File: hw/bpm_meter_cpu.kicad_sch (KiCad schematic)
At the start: 33 parts, among them J1 USB_C_Receptacle_USB2.0, J2 Conn_01x03_Pin, SW2 SW_MEC_5E, U1 RP2040, U3 W25Q128JVS, U4 AMS1117-3.3, Y1 Crystal_GND24_Small

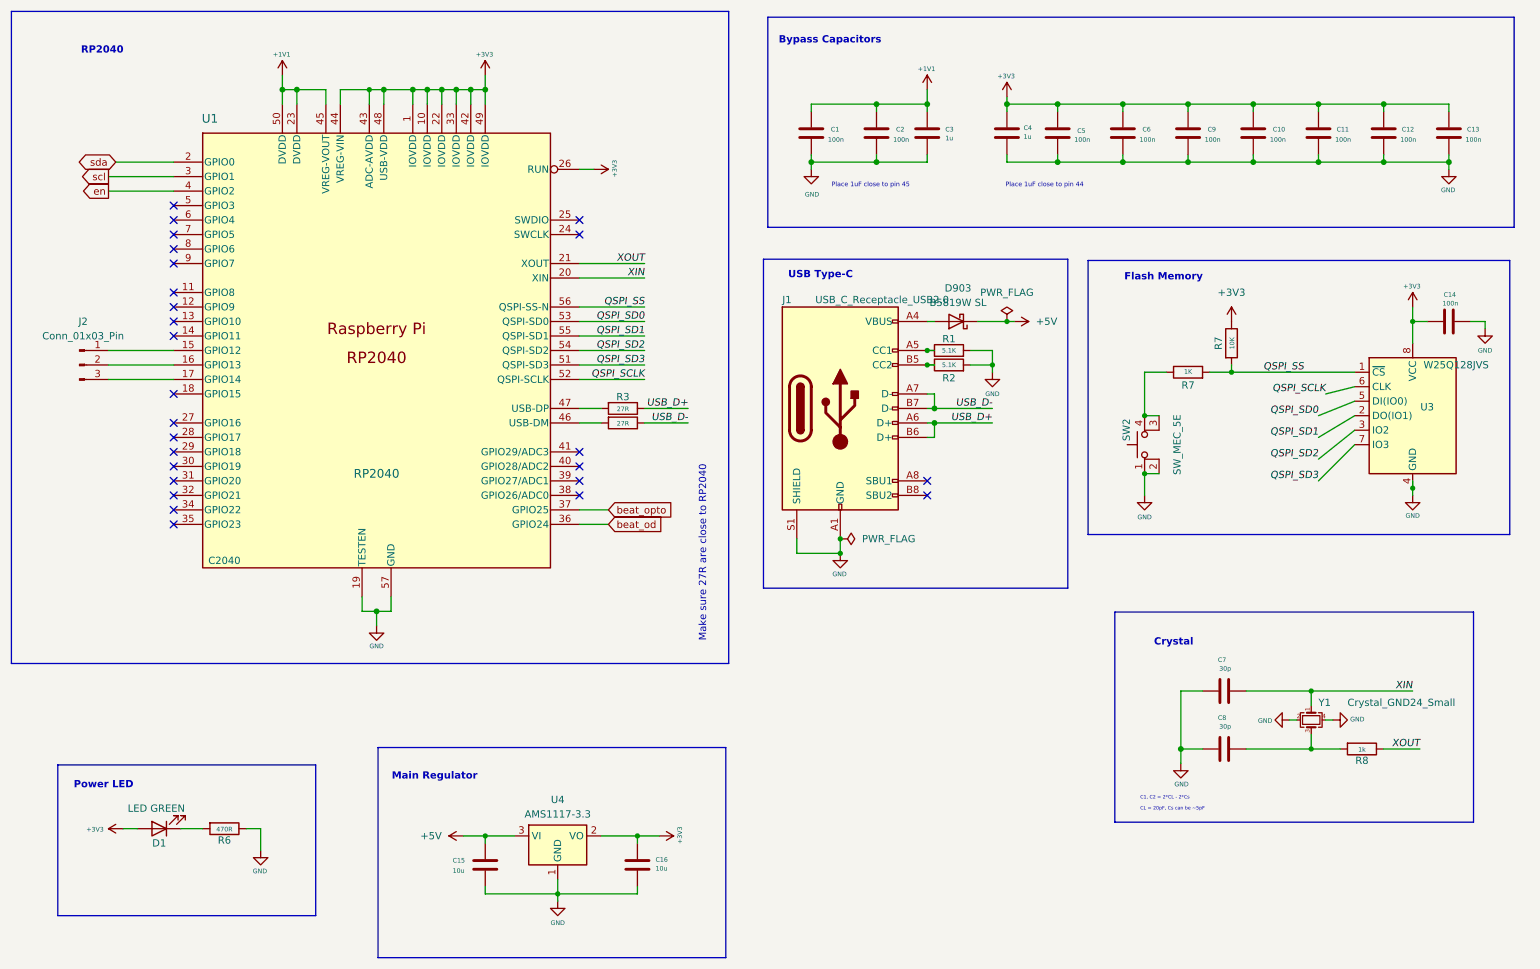
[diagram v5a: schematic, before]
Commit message: Changed LED driver to ISSI IS31FL3236A
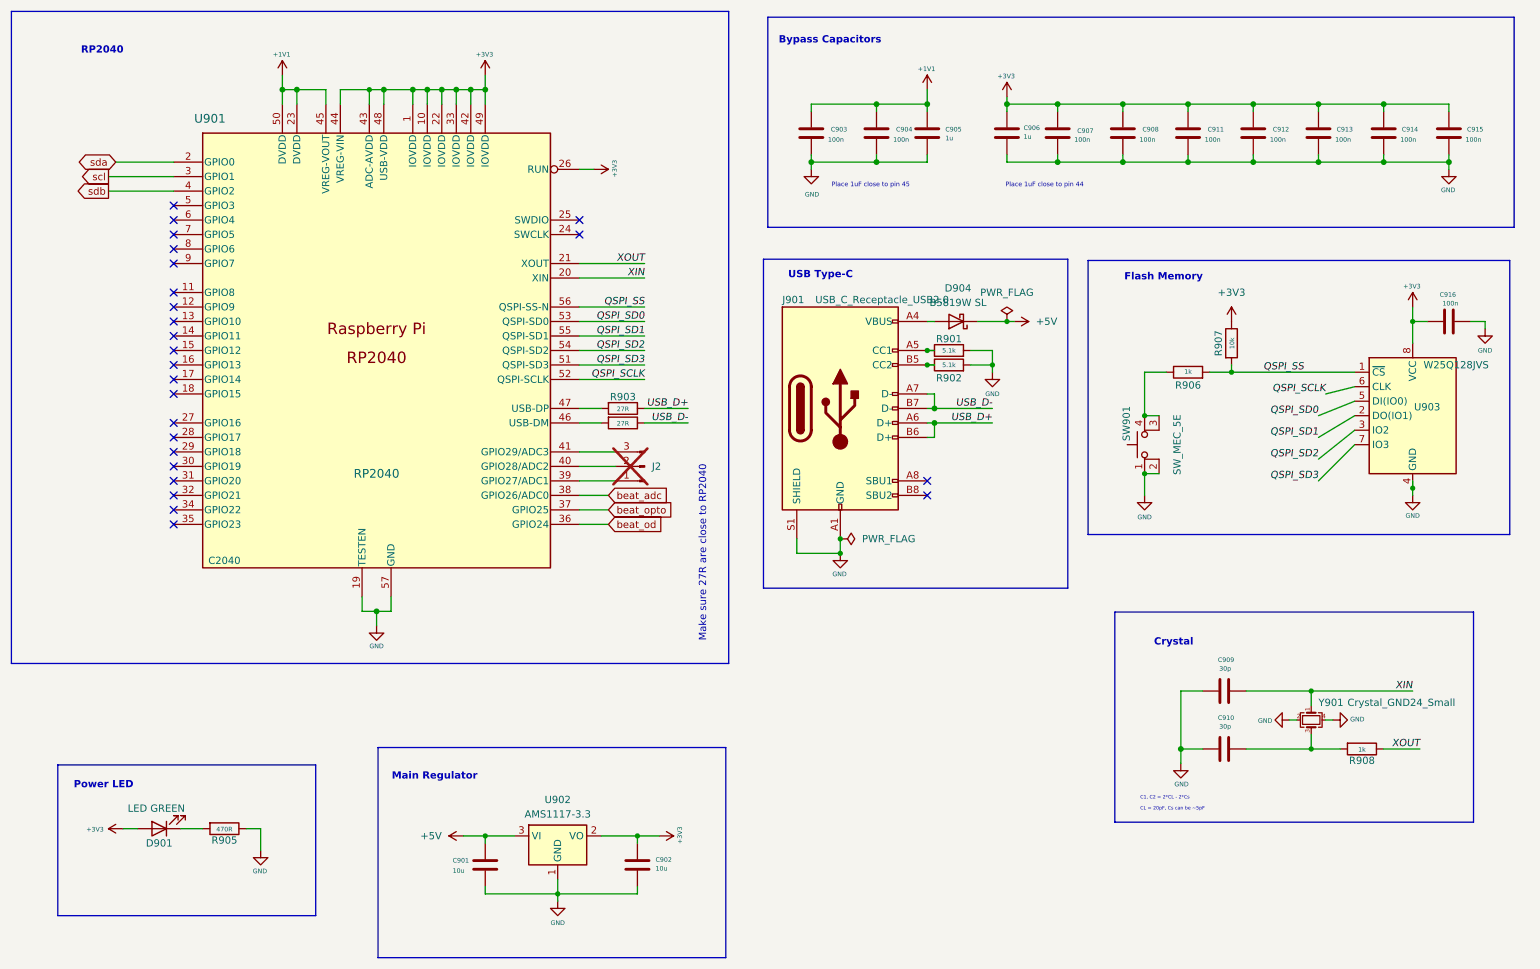
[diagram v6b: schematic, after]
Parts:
- J2: now not fitted
- R901: renamed from R1; value 5.1K -> 5.1k
- R902: renamed from R2; value 5.1K -> 5.1k
- R906: renamed from R7; value 1K -> 1k
- R907: renamed from R7; value 10K -> 10k
- U903: renamed from U3; JCL C97521 -> (none)
- renumbered C15 to C901, C16 to C902, C1 to C903, C2 to C904, C3 to C905, C4 to C906, C5 to C907, C6 to C908, C7 to C909, C8 to C910, C9 to C911, C10 to C912, C11 to C913, C12 to C914, C13 to C915, C14 to C916, D1 to D901, D903 to D904, J1 to J901, R3 to R903, R4 to R904, R6 to R905, R8 to R908, SW2 to SW901, U1 to U901, U4 to U902, Y1 to Y901
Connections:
- net at J2.1 (Pin_1): now also U901.39 (GPIO27/ADC1); no longer U901.15 (GPIO12)
- net at J2.2 (Pin_2): now also U901.40 (GPIO28/ADC2); no longer U901.16 (GPIO13)
- net at J2.3 (Pin_3): now also U901.41 (GPIO29/ADC3); no longer U901.17 (GPIO14)
- net beat_adc: now reaches U901.38 (GPIO26/ADC0)
- net en renamed sdb
- no-connect marks 26 -> 25

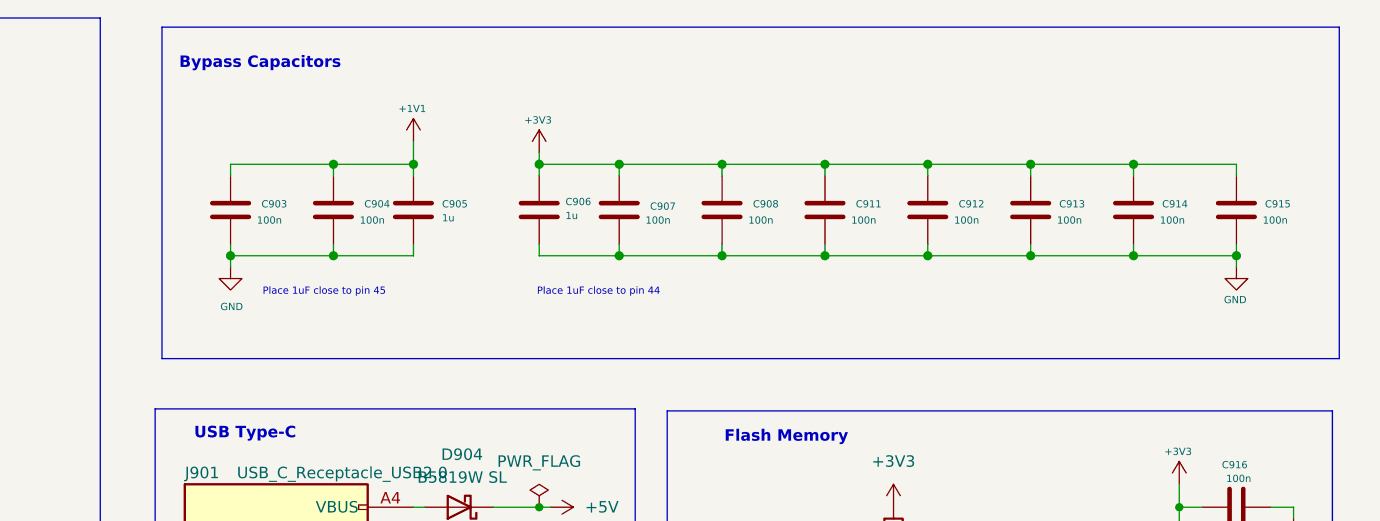
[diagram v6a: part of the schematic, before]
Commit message: Optimized layout of the RP2040
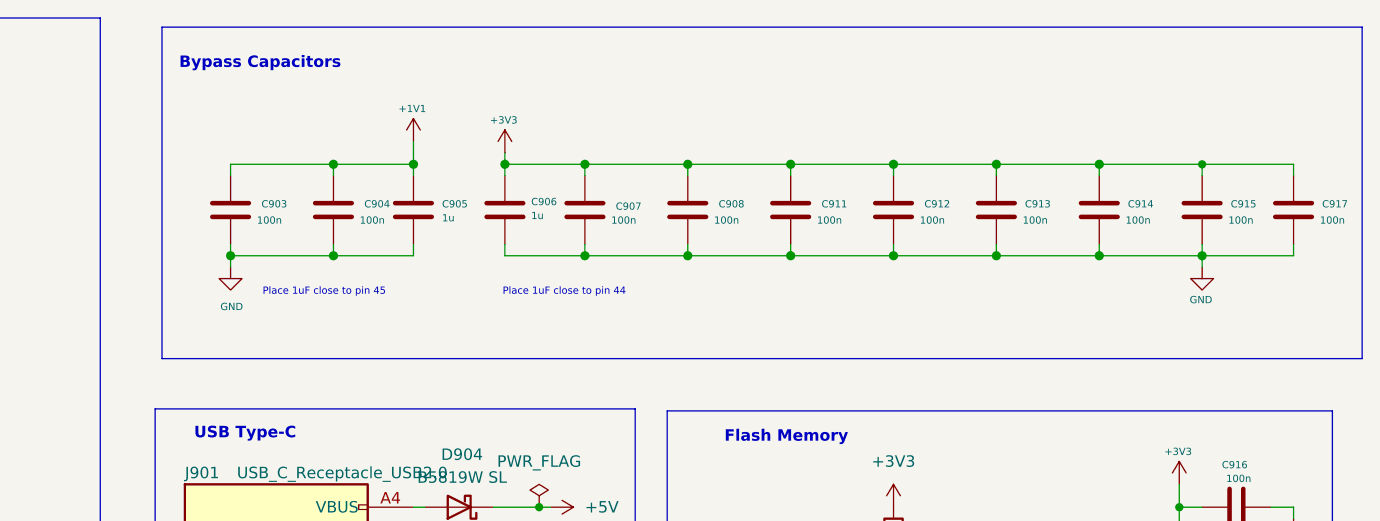
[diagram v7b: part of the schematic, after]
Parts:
- added C917: 100n, Capacitor_SMD:C_0402_1005Metric_Pad0.74x0.62mm_HandSolder, symbol 00_project_library:C
- D901: footprint 00_project_library:LED_0603_1608Metric -> LED_SMD:LED_0805_2012Metric
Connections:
- net +3V3: now also C917.1
- net GND: now also C917.2
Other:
- moved on the sheet: C906, C907, C908, C911, C912, C913, C914, C915

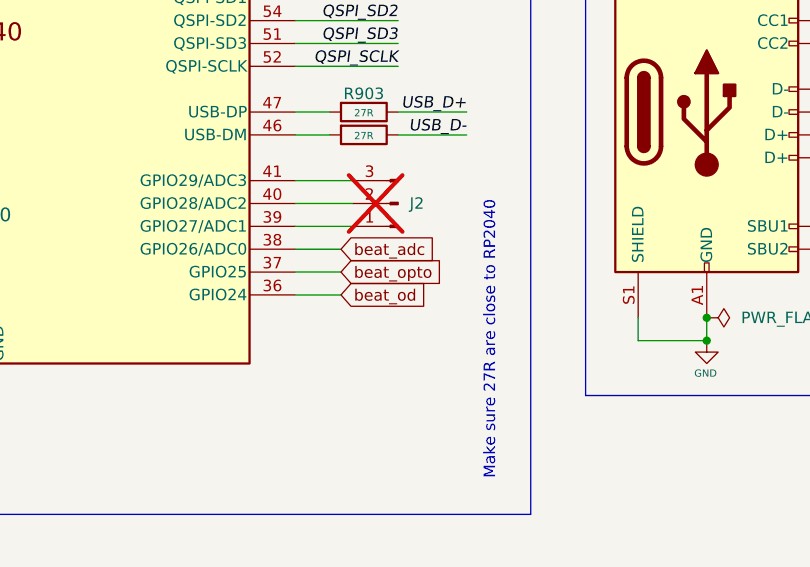
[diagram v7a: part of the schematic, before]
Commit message: Routing almost finished, QSPI flash missing
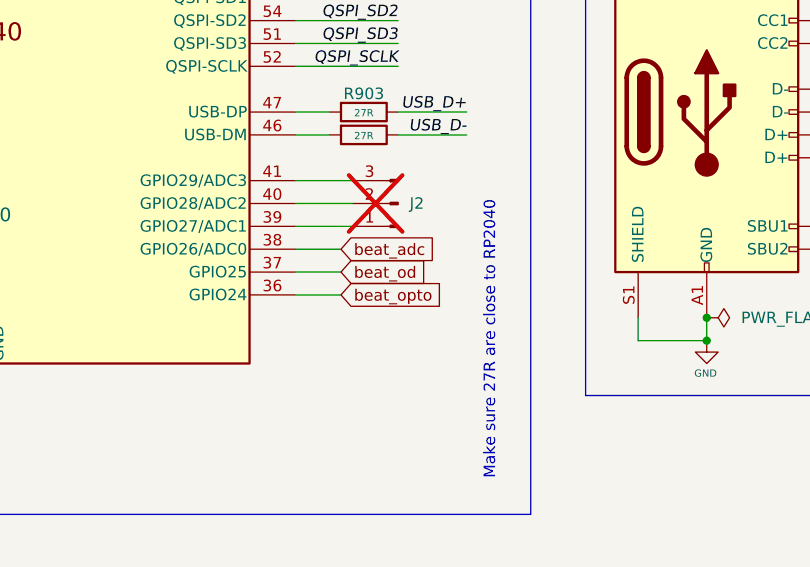
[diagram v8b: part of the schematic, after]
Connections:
- net beat_od: now also U901.37 (GPIO25); no longer U901.36 (GPIO24)
- net beat_opto: now also U901.36 (GPIO24); no longer U901.37 (GPIO25)
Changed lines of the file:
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@@
   (no_connect (at 44.45 100.33))
   (no_connect (at 44.45 74.93))
+  (wire (pts (xy 115.57 105.41) (xy 120.65 105.41))
+    (stroke (width 0) (type default))
+  )
   (wire (pts (xy 99.06 31.75) (xy 99.06 29.21))
     (stroke (width 0) (type solid))
@@
     (stroke (width 0) (type default))
   )
-  (wire (pts (xy 115.57 105.41) (xy 120.65 105.41))
-    (stroke (width 0) (type default))
-  )
   (wire (pts (xy 184.15 74.93) (xy 187.96 74.93))
     (stroke (width 0) (type default))
@@
     (stroke (width 0) (type solid))
   )
+  (wire (pts (xy 63.5 26.67) (xy 63.5 29.21))
+    (stroke (width 0) (type solid))
+  )
+  (wire (pts (xy 66.04 31.75) (xy 66.04 29.21))
+    (stroke (width 0) (type solid))
+  )
+  (wire (pts (xy 274.32 69.85) (xy 274.32 71.12))
+    (stroke (width 0) (type default))
+  )
+  (wire (pts (xy 127 85.09) (xy 134.62 85.09))
+    (stroke (width 0) (type solid))
+  )
+  (wire (pts (xy 77.47 120.65) (xy 77.47 118.11))
+    (stroke (width 0) (type solid))
+  )
+  (wire (pts (xy 214.63 100.33) (xy 214.63 96.52))
+    (stroke (width 0) (type default))
+  )
+  (wire (pts (xy 243.84 142.24) (xy 243.84 144.78))
+    (stroke (width 0) (type default))
+  )
+  (wire (pts (xy 86.36 31.75) (xy 86.36 29.21))
+    (stroke (width 0) (type solid))
+  )
+  (wire (pts (xy 241.3 33.02) (xy 241.3 31.75))
+    (stroke (width 0) (type solid))
+  )
+  (wire (pts (xy 161.29 107.95) (xy 161.29 110.49))
+    (stroke (width 0) (type solid))
+  )
+  (wire (pts (xy 153.67 110.49) (xy 161.29 110.49))
+    (stroke (width 0) (type solid))
+  )
+  (wire (pts (xy 44.45 44.45) (xy 33.02 44.45))
+    (stroke (width 0) (type default))
+  )
+  (wire (pts (xy 251.46 81.28) (xy 246.38 82.55))
+    (stroke (width 0) (type default))
+  )
+  (wire (pts (xy 224.79 144.78) (xy 220.98 144.78))
+    (stroke (width 0) (type solid))
+  )
+  (wire (pts (xy 264.16 33.02) (xy 264.16 31.75))
+    (stroke (width 0) (type solid))
+  )
+  (wire (pts (xy 176.53 29.21) (xy 176.53 31.75))
+    (stroke (width 0) (type solid))
+  )
+  (wire (pts (xy 73.66 31.75) (xy 73.66 29.21))
+    (stroke (width 0) (type solid))
+  )
+  (wire (pts (xy 261.62 67.31) (xy 261.62 69.85))
+    (stroke (width 0) (type solid))
+  )
+  (wire (pts (xy 240.03 139.7) (xy 241.3 139.7))
+    (stroke (width 0) (type default))
+  )
+  (wire (pts (xy 186.69 31.75) (xy 195.58 31.75))
+    (stroke (width 0) (type solid))
+  )
+  (wire (pts (xy 186.69 41.91) (xy 195.58 41.91))
+    (stroke (width 0) (type solid))
+  )
+  (wire (pts (xy 224.79 134.62) (xy 220.98 134.62))
+    (stroke (width 0) (type solid))
+  )
+  (wire (pts (xy 111.76 167.64) (xy 111.76 170.18))
+    (stroke (width 0) (type default))
+  )
   (wire (pts (xy 115.57 102.87) (xy 120.65 102.87))
-    (stroke (width 0) (type default))
-  )
-  (wire (pts (xy 63.5 26.67) (xy 63.5 29.21))
-    (stroke (width 0) (type solid))
-  )
-  (wire (pts (xy 66.04 31.75) (xy 66.04 29.21))
-    (stroke (width 0) (type solid))
-  )
-  (wire (pts (xy 274.32 69.85) (xy 274.32 71.12))
-    (stroke (width 0) (type default))
-  )
-  (wire (pts (xy 127 85.09) (xy 134.62 85.09))
-    (stroke (width 0) (type solid))
-  )
-  (wire (pts (xy 77.47 120.65) (xy 77.47 118.11))
-    (stroke (width 0) (type solid))
-  )
-  (wire (pts (xy 214.63 100.33) (xy 214.63 96.52))
-    (stroke (width 0) (type default))
-  )
-  (wire (pts (xy 243.84 142.24) (xy 243.84 144.78))
-    (stroke (width 0) (type default))
-  )
-  (wire (pts (xy 86.36 31.75) (xy 86.36 29.21))
-    (stroke (width 0) (type solid))
-  )
-  (wire (pts (xy 241.3 33.02) (xy 241.3 31.75))
-    (stroke (width 0) (type solid))
-  )
-  (wire (pts (xy 161.29 107.95) (xy 161.29 110.49))
-    (stroke (width 0) (type solid))
-  )
-  (wire (pts (xy 153.67 110.49) (xy 161.29 110.49))
-    (stroke (width 0) (type solid))
-  )
-  (wire (pts (xy 44.45 44.45) (xy 33.02 44.45))
-    (stroke (width 0) (type default))
-  )
-  (wire (pts (xy 251.46 81.28) (xy 246.38 82.55))
-    (stroke (width 0) (type default))
-  )
-  (wire (pts (xy 224.79 144.78) (xy 220.98 144.78))
-    (stroke (width 0) (type solid))
-  )
-  (wire (pts (xy 264.16 33.02) (xy 264.16 31.75))
-    (stroke (width 0) (type solid))
-  )
-  (wire (pts (xy 176.53 29.21) (xy 176.53 31.75))
-    (stroke (width 0) (type solid))
-  )
-  (wire (pts (xy 73.66 31.75) (xy 73.66 29.21))
-    (stroke (width 0) (type solid))
-  )
-  (wire (pts (xy 261.62 67.31) (xy 261.62 69.85))
-    (stroke (width 0) (type solid))
-  )
-  (wire (pts (xy 240.03 139.7) (xy 241.3 139.7))
-    (stroke (width 0) (type default))
-  )
-  (wire (pts (xy 186.69 31.75) (xy 195.58 31.75))
-    (stroke (width 0) (type solid))
-  )
-  (wire (pts (xy 186.69 41.91) (xy 195.58 41.91))
-    (stroke (width 0) (type solid))
-  )
-  (wire (pts (xy 224.79 134.62) (xy 220.98 134.62))
-    (stroke (width 0) (type solid))
-  )
-  (wire (pts (xy 111.76 167.64) (xy 111.76 170.18))
     (stroke (width 0) (type default))
   )
@@
     )
   )
-  (global_label "beat_od" (shape input) (at 120.65 105.41 0) (fields_autoplaced)
+  (global_label "beat_od" (shape input) (at 120.65 102.87 0) (fields_autoplaced)
     (effects (font (size 1.27 1.27)) (justify left))
-    (property "Intersheetrefs" "${INTERSHEET_REFS}" (at 131.1082 105.41 0)
+    (property "Intersheetrefs" "${INTERSHEET_REFS}" (at 131.1082 102.87 0)
       (effects (font (size 1.27 1.27)) (justify left) hide)
     )
@@
     )
   )
-  (global_label "beat_opto" (shape input) (at 120.65 102.87 0) (fields_autoplaced)
+  (global_label "beat_opto" (shape input) (at 120.65 105.41 0) (fields_autoplaced)
     (effects (font (size 1.27 1.27)) (justify left))
-    (property "Intersheetrefs" "${INTERSHEET_REFS}" (at 132.9829 102.87 0)
+    (property "Intersheetrefs" "${INTERSHEET_REFS}" (at 132.9829 105.41 0)
       (effects (font (size 1.27 1.27)) (justify left) hide)
     )
